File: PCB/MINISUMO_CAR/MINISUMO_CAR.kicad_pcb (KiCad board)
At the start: 2 copper layers, 40 x 50 mm, 1 part

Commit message: PCB
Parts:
- added TP1: Positive, TestPoint:TestPoint_THTPad_3.0x3.0mm_Drill1.5mm, F.Cu at (136.5, 117.4)
- added TP3: Negative, TestPoint:TestPoint_THTPad_3.0x3.0mm_Drill1.5mm, F.Cu at (148.3, 117.3)
- added U2: L298N, EasyEDA:L298N-module-43x43mm, F.Cu at (177.2, 89.8)
- moved A1 1.27 mm to (151.1, 111.0)
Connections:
- A1 pad 29: unconnected-(A1-GND-Pad29) -> -BATT
- A1 pad 30: unconnected-(A1-VIN-Pad30) -> +BATT
- A1 pad 4: unconnected-(A1-GND-Pad4) -> -BATT

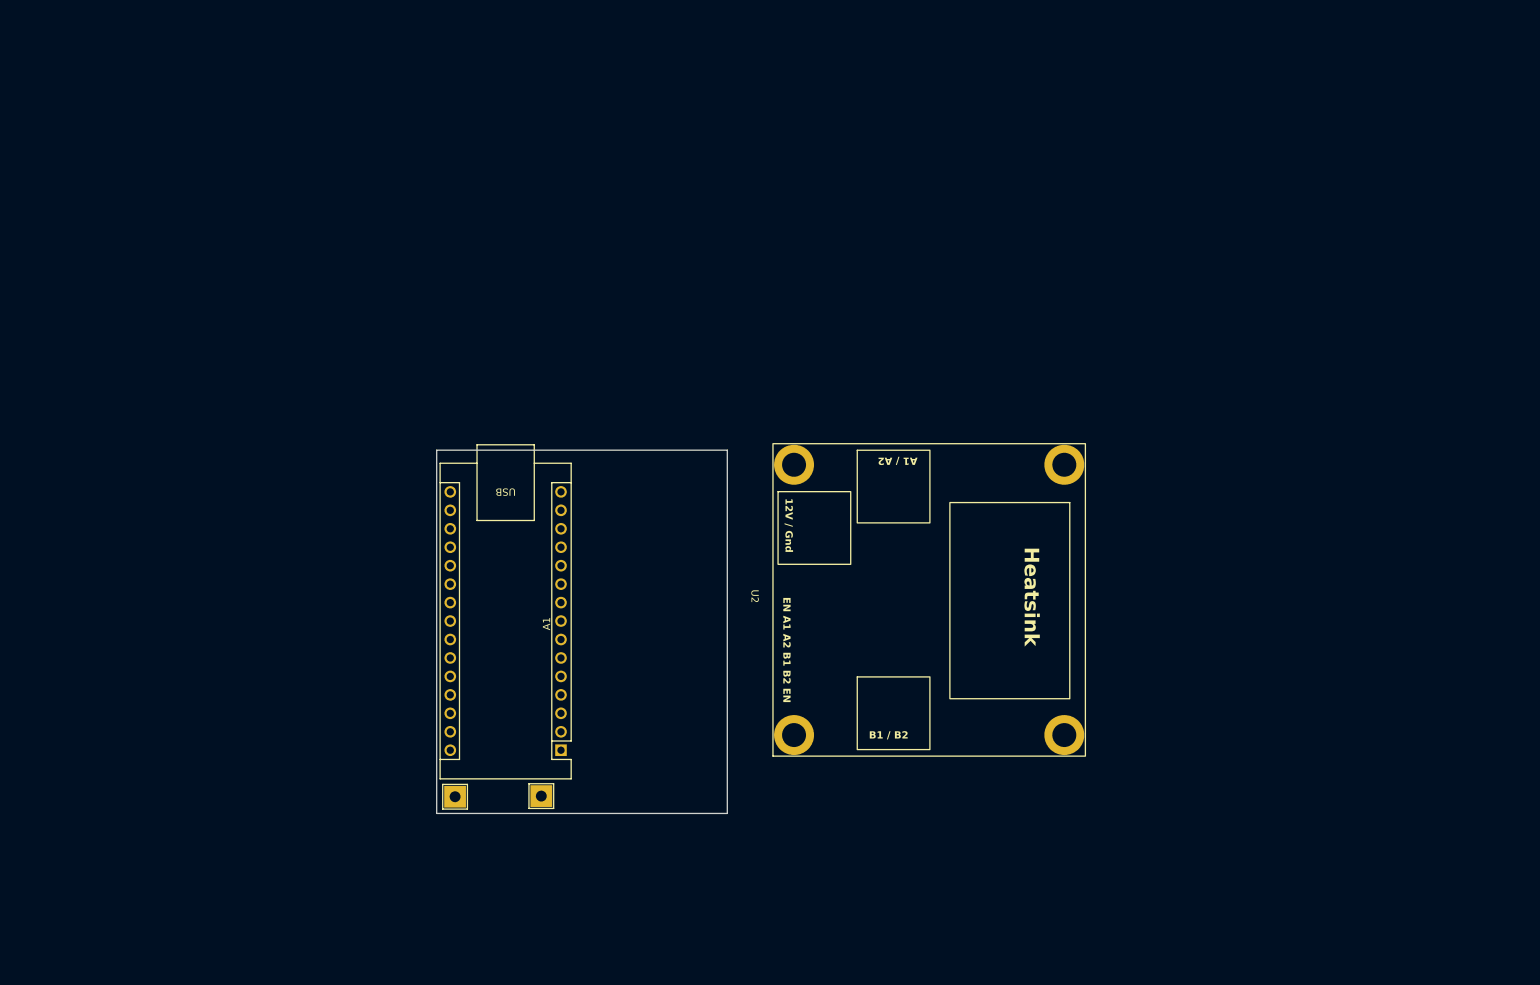
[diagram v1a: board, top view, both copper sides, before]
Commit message: add sensors  HC-SR04
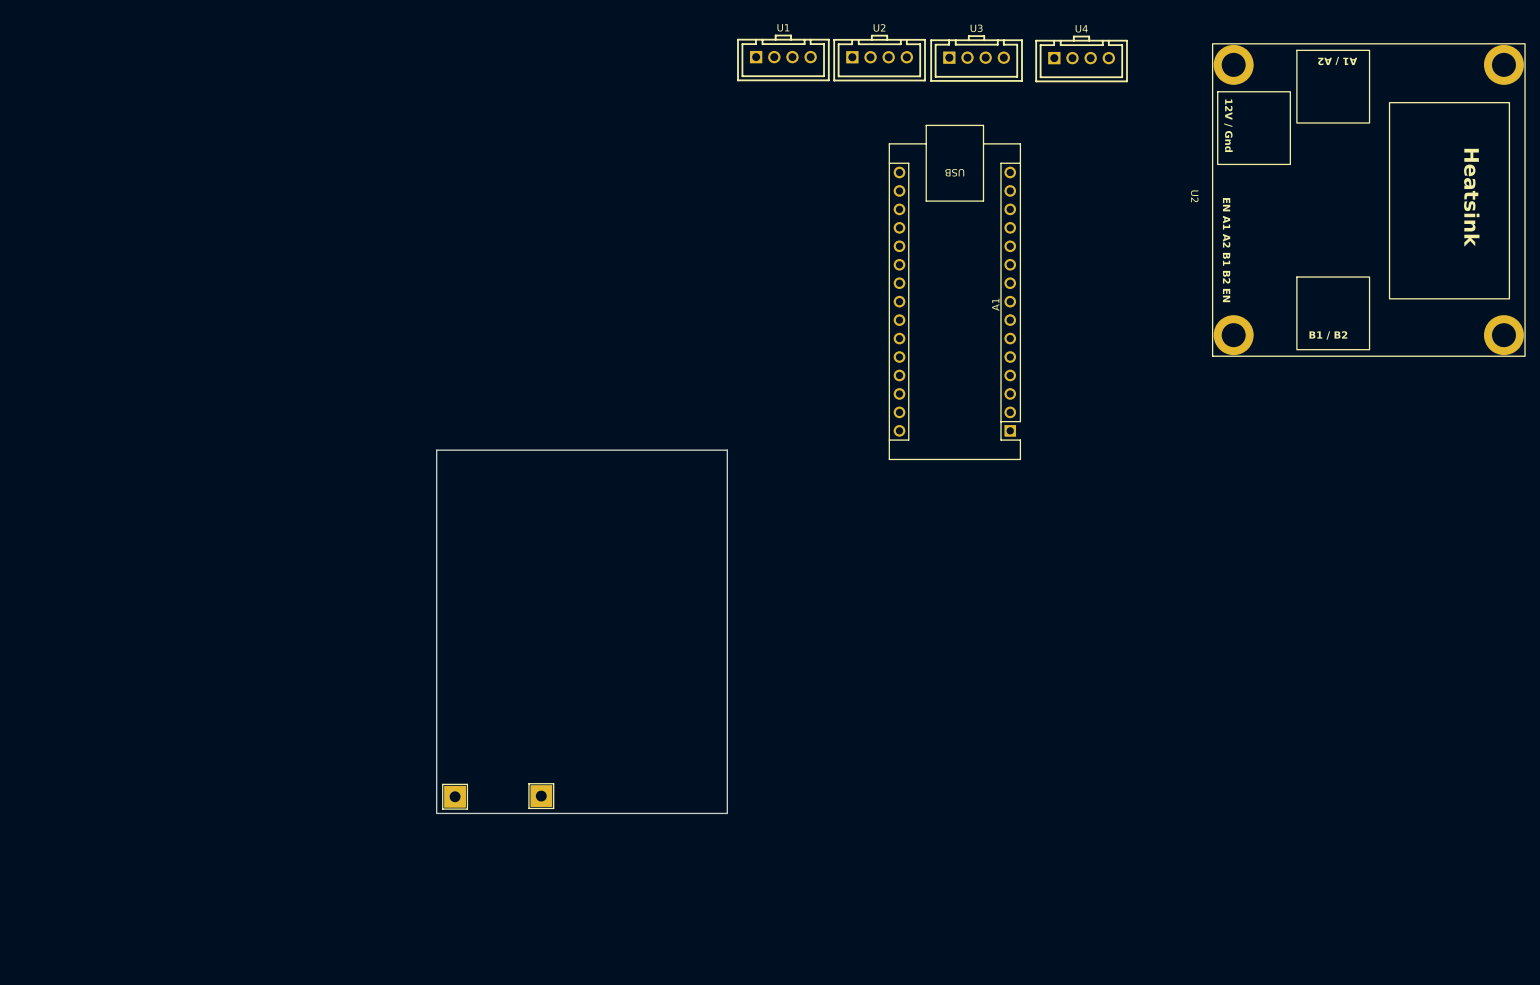
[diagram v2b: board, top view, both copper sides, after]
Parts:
- added U1: XY-XHB2.54-4A11, EasyEDA:HDR-TH_4P-P2.50-V-F-2, F.Cu at (181.7, 15.6)
- added U2: XY-XHB2.54-4A11, EasyEDA:HDR-TH_4P-P2.50-V-F-2, F.Cu at (194.9, 15.6)
- added U3: XY-XHB2.54-4A11, EasyEDA:HDR-TH_4P-P2.50-V-F-2, F.Cu at (208.3, 15.7)
- added U4: XY-XHB2.54-4A11, EasyEDA:HDR-TH_4P-P2.50-V-F-2, F.Cu at (222.7, 15.7)
- moved U2 81.8 mm to (237.7, 34.8)
- moved A1 75.9 mm to (212.9, 67.0)

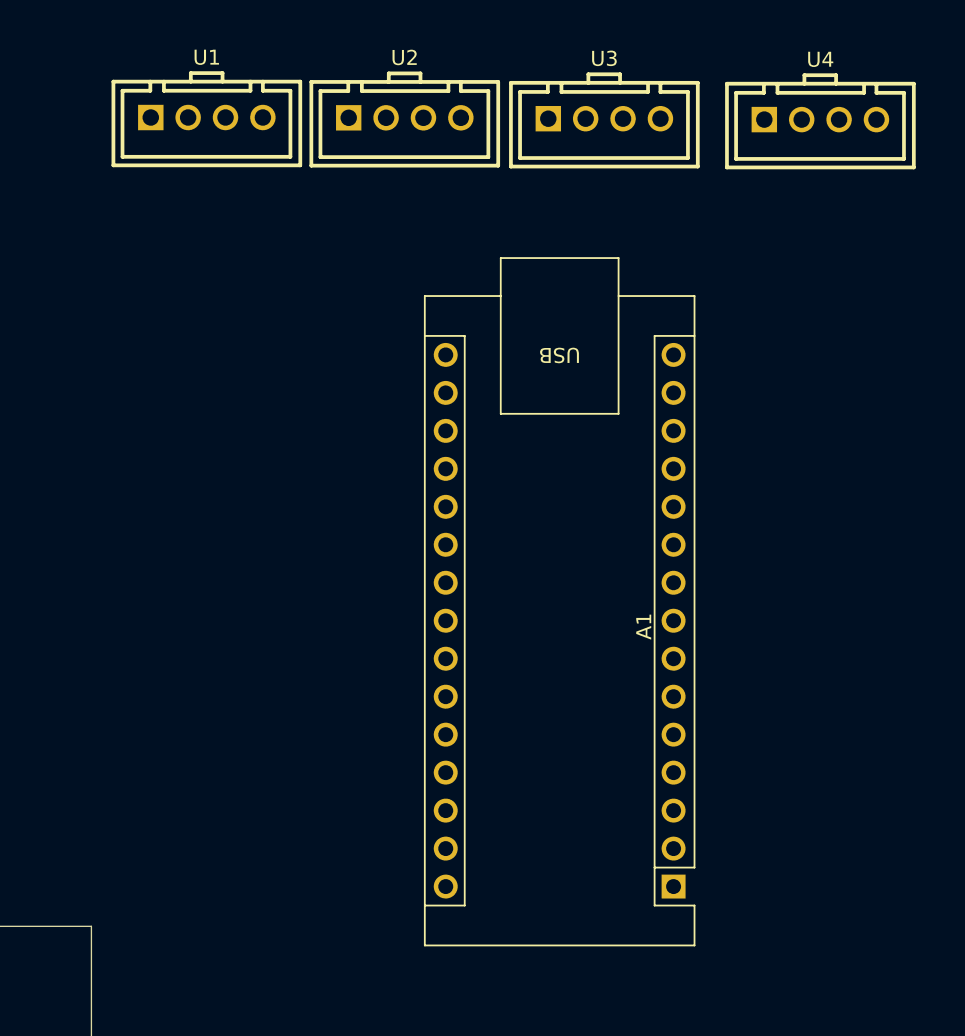
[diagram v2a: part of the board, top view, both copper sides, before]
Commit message: add sensor infrarojo
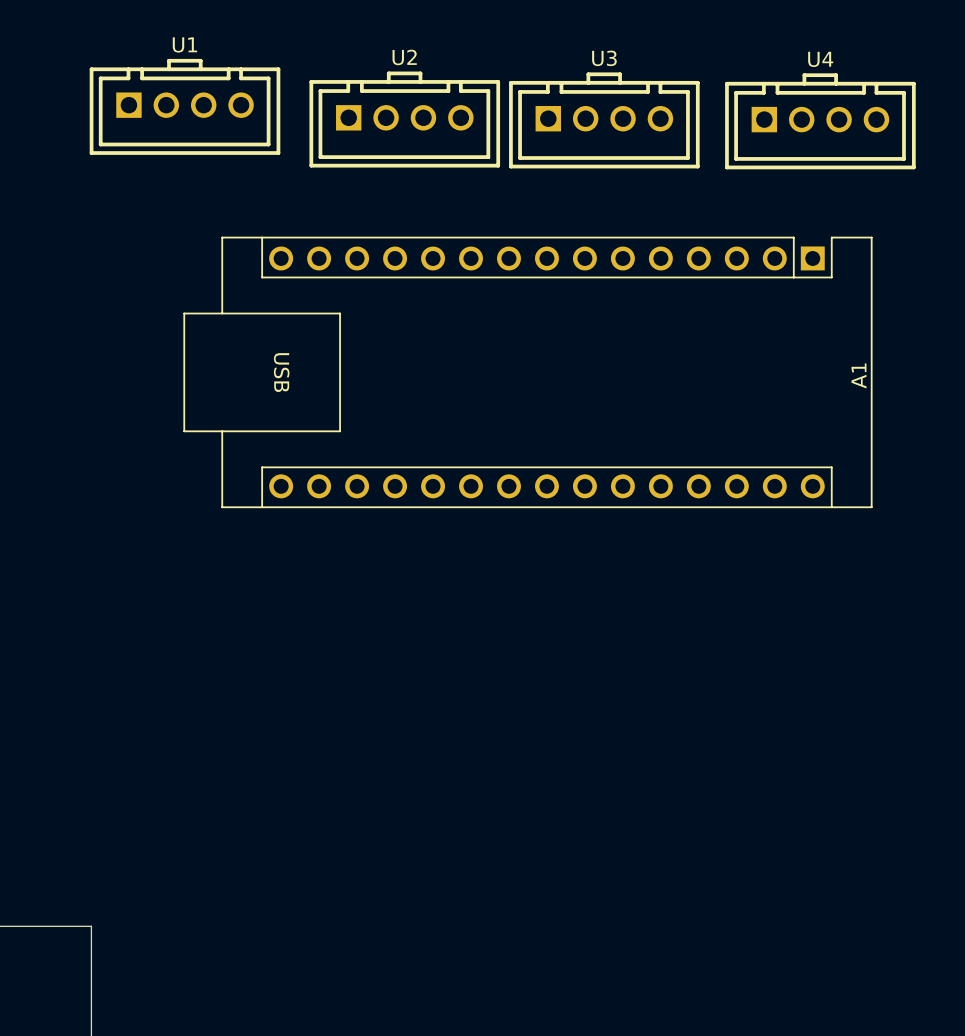
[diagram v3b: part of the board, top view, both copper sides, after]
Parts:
- moved A1 43.0 mm to (222.2, 25.0), turned to -90 degrees
- moved U1 1.68 mm to (180.2, 14.8)
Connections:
- U1 pad 1: unconnected-(U1-Pad1) -> Net-(JP1-A)
- U1 pad 2: unconnected-(U1-Pad2) -> /TRIG
- U1 pad 3: unconnected-(U1-Pad3) -> /ECHO
- U2 pad 1: unconnected-(U2-Pad1) -> Net-(JP1-A)
- U2 pad 2: unconnected-(U2-Pad2) -> /TRIG1
- U2 pad 3: unconnected-(U2-Pad3) -> /ECHO1
- U3 pad 1: unconnected-(U3-Pad1) -> Net-(JP1-A)
- U3 pad 2: unconnected-(U3-Pad2) -> /TRIG2
- U3 pad 3: unconnected-(U3-Pad3) -> /ECHO2
- U4 pad 1: unconnected-(U4-Pad1) -> Net-(JP1-A)
- U4 pad 2: unconnected-(U4-Pad2) -> /TRIG3
- U4 pad 3: unconnected-(U4-Pad3) -> /ECHO3

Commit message: Finish to day 7_27_2026
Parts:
- added GND1: PH_GND, Connector_PinHeader_2.00mm:PinHeader_1x01_P2.00mm_Vertical, F.Cu at (79.0, 100.0)
- added INA1: INA1, Connector_PinHeader_2.00mm:PinHeader_1x01_P2.00mm_Vertical, F.Cu at (79.0, 109.3)
- added INA2: INA2, Connector_PinHeader_2.00mm:PinHeader_1x01_P2.00mm_Vertical, F.Cu at (83.5, 109.2)
- added INB1: INB1, Connector_PinHeader_2.00mm:PinHeader_1x01_P2.00mm_Vertical, F.Cu at (79.0, 106.2)
- added INB2: INB2, Connector_PinHeader_2.00mm:PinHeader_1x01_P2.00mm_Vertical, F.Cu at (83.5, 106.1)
- added PWM1: PWM, Connector_PinHeader_2.00mm:PinHeader_1x01_P2.00mm_Vertical, F.Cu at (83.5, 100.0)
- added PWM2: PWM, Connector_PinHeader_2.00mm:PinHeader_1x01_P2.00mm_Vertical, F.Cu at (83.5, 103.0)
- added U5: XY-XHB2.54-3A11, EasyEDA:CONN-TH_3P-P2.50_XY-XHB2.54-3A11, B.Cu at (107.2, 100.4)
- added U6: XY-XHB2.54-3A11, EasyEDA:CONN-TH_3P-P2.50_XY-XHB2.54-3A11, B.Cu at (115.5, 100.5)
- added VCC1: M_VCC, Connector_PinHeader_2.00mm:PinHeader_1x01_P2.00mm_Vertical, F.Cu at (79.0, 103.1)
- U2: moved to B.Cu
- moved A1 164.1 mm to (102.3, 137.1), turned to 180 degrees
- moved U3 154.2 mm to (111.3, 135.6)
- moved U2 147.1 mm to (116.0, 117.3), turned to 90 degrees
- moved U1 143.0 mm to (80.8, 117.6), turned to -90 degrees
- moved U2 120.0 mm to (111.3, 101.7), turned to 90 degrees
- moved U4 119.9 mm to (158.5, 117.0), turned to 90 degrees
- moved TP3 68.5 mm to (80.8, 128.6)
- moved TP1 58.9 mm to (80.8, 136.4)
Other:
- board size 40 x 50 mm -> 85 x 44 mm

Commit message: update of sensor v3
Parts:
- added 5v1: 5v, Connector_PinHeader_2.00mm:PinHeader_1x01_P2.00mm_Vertical, F.Cu at (89.3, 129.1)
- added C1: 100nf, Capacitor_SMD:C_0805_2012Metric, B.Cu at (85.4, 128.7)
- added C3: 0.33uF, Capacitor_SMD:C_0805_2012Metric, B.Cu at (80.0, 105.5)
- added C4: 470uf, Capacitor_SMD:CP_Elec_10x10.5, B.Cu at (82.6, 116.5)
- added C5: 0.1uF, Capacitor_SMD:C_0805_2012Metric, B.Cu at (89.1, 98.1)
- added C6: 0.1uF, Capacitor_SMD:C_0805_2012Metric, B.Cu at (79.8, 102.1)
- added C7: 100uF, Capacitor_SMD:CP_Elec_6.3x7.7, B.Cu at (86.5, 105.4)
- added GND2: PH_GND, Connector_PinHeader_2.00mm:PinHeader_1x01_P2.00mm_Vertical, F.Cu at (122.8, 107.6)
- added R1: 10k, Resistor_SMD:R_0805_2012Metric_Pad1.20x1.40mm_HandSolder, B.Cu at (100.0, 118.5)
- added SW1: SW_Push, Button_Switch_THT:SW_PUSH_6mm_H5mm, F.Cu at (87.7, 125.5)
- added THECPCENTER: LOGO, images:IMG1, F.Cu at (86.6, 115.3)
- added U14: LM7805_TO220, Package_TO_SOT_THT:TO-220-3_Vertical, F.Cu at (79.9, 98.6)
- added pin_libre1: pin_libre, Connector_PinHeader_2.00mm:PinHeader_1x01_P2.00mm_Vertical, F.Cu at (96.7, 122.5)
- moved U4 45.1 mm to (115.3, 103.6), turned to -90 degrees
- moved VCC1 39.0 mm to (99.0, 136.6)
- moved U1 36.4 mm to (115.3, 129.3), turned to 180 degrees
- moved TP3 33.4 mm to (113.6, 135.0)
- moved GND1 33.0 mm to (103.0, 122.7)
- moved PWM2 27.2 mm to (110.5, 99.2)
- moved PWM1 27.1 mm to (110.3, 103.4)
- moved U3 22.6 mm to (115.8, 113.4), turned to 180 degrees
- moved U2 21.4 mm to (115.4, 122.7), turned to 180 degrees
- moved INB1 19.2 mm to (96.4, 114.2)
- moved INB2 17.3 mm to (96.4, 117.7)
- moved INA1 16.7 mm to (95.6, 107.9)
- moved U6 16.3 mm to (99.3, 99.1), turned to 180 degrees
- moved INA2 12.8 mm to (96.2, 111.0)
- moved U5 9.86 mm to (102.1, 108.8), turned to -90 degrees
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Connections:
- A1 pad 10: unconnected-(A1-D7-Pad10) -> /ECHO2
- A1 pad 11: unconnected-(A1-D8-Pad11) -> /ECHO3
- A1 pad 12: unconnected-(A1-D9-Pad12) -> /TRIG3
- A1 pad 13: unconnected-(A1-D10-Pad13) -> /D10
- A1 pad 14: unconnected-(A1-D11-Pad14) -> /D11
- A1 pad 15: unconnected-(A1-D12-Pad15) -> /OUT
- A1 pad 16: unconnected-(A1-D13-Pad16) -> /OUT1
- A1 pad 17: unconnected-(A1-3V3-Pad17) -> 3+
- A1 pad 19: unconnected-(A1-A0-Pad19) -> /A0
- A1 pad 20: unconnected-(A1-A1-Pad20) -> /A1
- A1 pad 21: unconnected-(A1-A2-Pad21) -> /A2
- A1 pad 22: unconnected-(A1-A3-Pad22) -> /A3
- A1 pad 23: unconnected-(A1-A4-Pad23) -> /A4
- A1 pad 24: unconnected-(A1-A5-Pad24) -> /A5
- A1 pad 27: unconnected-(A1-+5V-Pad27) -> Net-(A1-+5V)
- A1 pad 5: unconnected-(A1-D2-Pad5) -> /ECHO
- A1 pad 6: unconnected-(A1-D3-Pad6) -> /TRIG
- A1 pad 7: unconnected-(A1-D4-Pad7) -> /ECHO1
- A1 pad 8: unconnected-(A1-D5-Pad8) -> /TRIG1
- A1 pad 9: unconnected-(A1-D6-Pad9) -> /TRIG2
- INA1 pad 1: unconnected-(INA1-Pad1) -> /A0
- INA2 pad 1: unconnected-(INA2-Pad1) -> /A1
- INB1 pad 1: unconnected-(INB1-Pad1) -> /A2
- INB2 pad 1: unconnected-(INB2-Pad1) -> /A3
- PWM1 pad 1: unconnected-(PWM1-Pad1) -> /D10
- PWM2 pad 1: unconnected-(PWM2-Pad1) -> /D11
- U1 pad 1: Net-(JP1-A) -> 5+
- U2 pad 1: Net-(JP1-A) -> 5+
- U2 pad 1: (no net) -> -BATT
- U3 pad 1: Net-(JP1-A) -> 5+
- U4 pad 1: Net-(JP1-A) -> 5+
- U5 pad 2: Net-(JP2-A) -> 5+
- U6 pad 2: Net-(JP2-A) -> 5+
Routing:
- net -BATT: track 0.00 -> 167.6 mm
- net 5+: track 0.00 -> 102.5 mm
- net +BATT: track 0.00 -> 61.9 mm
- net /A4: track 0.00 -> 28.7 mm
- net /TRIG: track 0.00 -> 13.0 mm
- net /TRIG2: track 0.00 -> 12.4 mm
- net /TRIG1: track 0.00 -> 12.3 mm
- net /OUT1: track 0.00 -> 11.4 mm
- net /ECHO3: track 0.00 -> 10.8 mm
- net /TRIG3: track 0.00 -> 10.8 mm
- net /ECHO2: track 0.00 -> 9.58 mm
- net /ECHO1: track 0.00 -> 9.41 mm
- net /ECHO: track 0.00 -> 9.02 mm
- net /OUT: track 0.00 -> 8.08 mm
- net /D11: track 0.00 -> 7.07 mm
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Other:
- board text added: "Paul Martinez 2024-1267 Alberto Méndez 2023-1969 Isaías Matos 2024-0688 Miguel Ramírez 2024-1264"
